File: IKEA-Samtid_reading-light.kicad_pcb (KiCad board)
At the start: 2 copper layers, 21 x 100 mm, 30 parts, among them IC1 ATTINY25-S, P1 CONN_2, U1 MCP1804-SOT23-5, U2 PT4115-SOT89-5

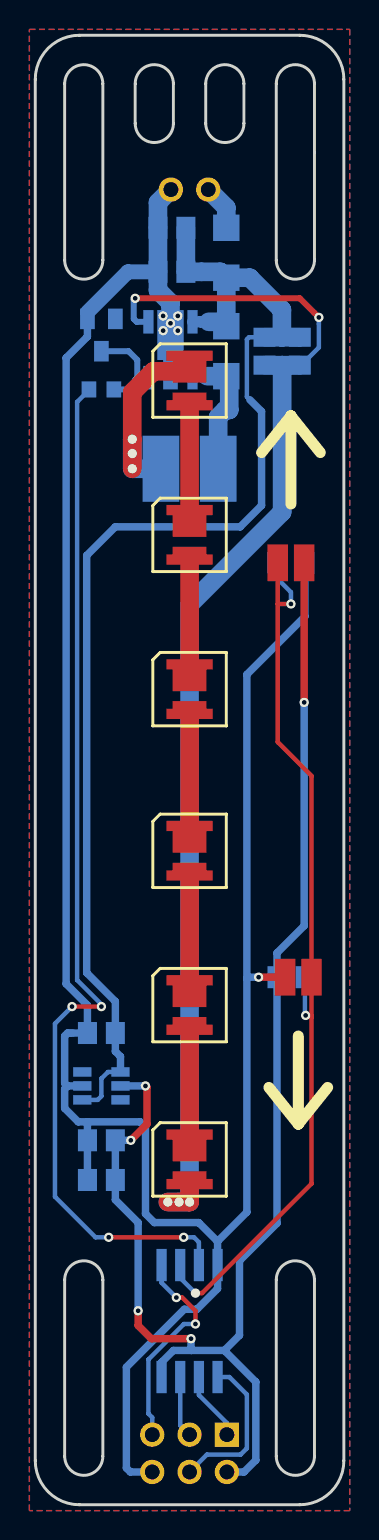
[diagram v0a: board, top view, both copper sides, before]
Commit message: Added a buffer-cap for the ADC input + minor layout tweaks.
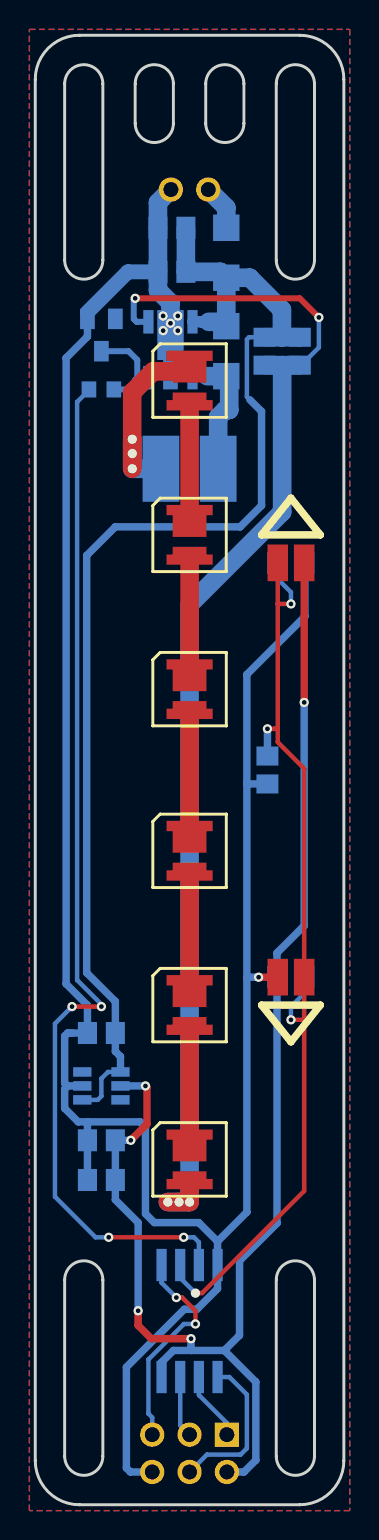
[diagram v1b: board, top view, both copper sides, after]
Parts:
- added C6: 100nF, my_parts:MADW__C0805, B.Cu at (76.3, 88.5)
- moved FSEN2 0.50 mm to (77.9, 102.6)
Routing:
- net /FSEN: track 63.7 -> 67.0 mm, vias 3 -> 4
- net GND: track 99.8 -> 100.8 mm

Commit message: Tweaks.
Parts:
- turned FSEN1 to 180 degrees
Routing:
- net /FSEN: track 67.0 -> 99.2 mm, vias 4 -> 2
- net GND: track 100.8 -> 102.2 mm
- net +5V: track 97.1 -> 98.1 mm
- net +24V: track 87.3 -> 86.3 mm

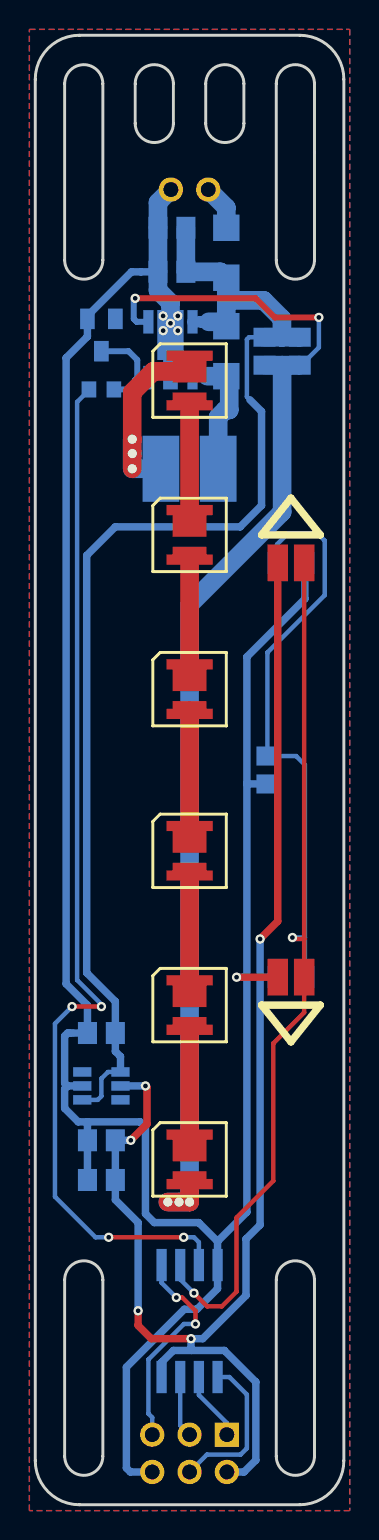
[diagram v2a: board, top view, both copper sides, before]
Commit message: Moved sensor pads away from LEDs + improved power input footprint.
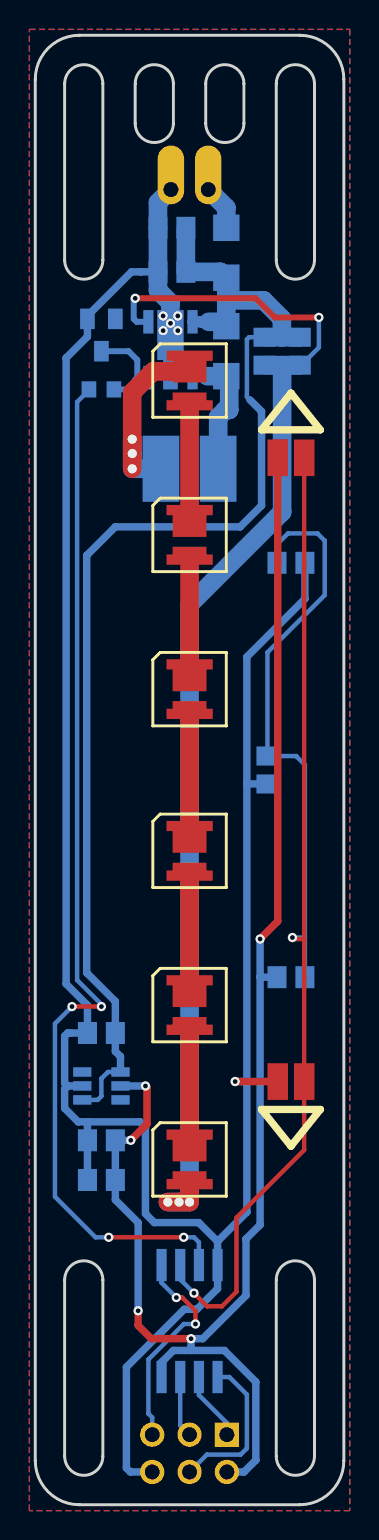
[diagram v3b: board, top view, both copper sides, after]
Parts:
- moved FSEN1 7.15 mm to (77.9, 67.2)
- moved FSEN2 7.10 mm to (77.9, 109.7)
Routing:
- net /FSEN: track 99.2 -> 106.4 mm
- net +5V: track 98.1 -> 105.3 mm
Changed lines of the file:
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@@
     (thickness 1.6002)
     (drawings 70)
-    (tracks 278)
+    (tracks 279)
     (zones 0)
     (modules 31)
@@
   )
   (setup
-    (last_trace_width 1.27)
+    (last_trace_width 0.2032)
     (user_trace_width 0.2032)
     (user_trace_width 0.3048)
@@
     (mod_text_size 1 1)
     (mod_text_width 0.2)
-    (pad_size 0.85 0.85)
-    (pad_drill 0.35)
+    (pad_size 4 1.8)
+    (pad_drill 1.016)
     (pad_to_mask_clearance 0)
     (aux_axis_origin 0 0)
@@
     (add_net "Net-(D6-Pad2)")
     (add_net "Net-(DS1-Pad1)")
+  )
+  (module my_parts:MADW__edge-connector_SIL2_male (layer Back)
+    (at 71 49 270)
+    (clearance 0.5)
+    (fp_text reference P1 (at 0 3.81 270) (layer B.SilkS) hide
+      (effects (font (size 1 1) (thickness 0.2)) (justify mirror))
+    )
+    (fp_text value CONN_2 (at 0 -3.81 270) (layer B.SilkS) hide
+      (effects (font (size 1 1) (thickness 0.2)) (justify mirror))
+    )
+    (fp_line (start -1.4 -2.54) (end -1.4 2.54) (layer B.SilkS) (width 0.2))
+    (fp_line (start -3.9 2.54) (end -3.9 -2.54) (layer B.SilkS) (width 0.2))
+    (fp_line (start -1.39954 2.54) (end -3.8989 2.54) (layer B.SilkS) (width 0.2))
+    (fp_line (start -3.8989 -1.27) (end -9.90092 -1.27) (layer B.SilkS) (width 0.2))
+    (fp_line (start -3.8989 1.27) (end -9.90092 1.27) (layer B.SilkS) (width 0.2))
+    (fp_line (start -1.39954 0) (end -3.8989 0) (layer B.SilkS) (width 0.2))
+    (fp_line (start -1.39954 -2.54) (end -3.8989 -2.54) (layer B.SilkS) (width 0.2))
+    (pad 2 thru_hole oval (at 0 -1.27 270) (size 4 1.8) (drill 1.016 (offset -1 0)) (layers *.Cu *.Mask B.SilkS)
+      (net 20 "Net-(DS1-Pad1)"))
+    (pad 1 thru_hole oval (at 0 1.27 270) (size 4 1.8) (drill 1.016 (offset -1 0)) (layers *.Cu *.Mask B.SilkS)
+      (net 19 GNDPWR) (zone_connect 1) (thermal_gap 0.5))
+    (model ../../../../../Arduino/KiCAD/kicad_sources/library-repos/kicad-library/modules/packages3d/Pin_Headers/Pin_Header_Angled_1x02.wrl
+      (at (xyz 0 0 0))
+      (scale (xyz 1 1 1))
+      (rotate (xyz 0 0 -90))
+    )
   )
   (module my_parts:MADW__SOT89-5 (layer Back)
@@
   )
   (module my_parts:MADW__SMD_2-pin_square_3.2x2.5mm (layer Front)
-    (at 77.9 102.6)
+    (at 77.9 109.7)
     (tags "CONN DEV")
     (clearance 0.4)
@@
   )
   (module my_parts:MADW__SMD_2-pin_square_3.2x2.5mm (layer Front)
-    (at 77.9 74.4 180)
+    (at 77.9 67.25 180)
     (tags "CONN DEV")
     (clearance 0.4)
@@
     (pad 1 smd rect (at 0.9 0 180) (size 1.4 2.5) (layers Front F.Paste F.Mask)
       (net 9 +5V))
-  )
-  (module my_parts:MADW__edge-connector_SIL2_male (layer Back)
-    (at 71 49 270)
-    (fp_text reference P1 (at 0 3.81 270) (layer B.SilkS) hide
-      (effects (font (size 1 1) (thickness 0.2)) (justify mirror))
-    )
-    (fp_text value CONN_2 (at 0 -3.81 270) (layer B.SilkS) hide
-      (effects (font (size 1 1) (thickness 0.2)) (justify mirror))
-    )
-    (fp_line (start -1.4 -2.54) (end -1.4 2.54) (layer B.SilkS) (width 0.2))
-    (fp_line (start -3.9 2.54) (end -3.9 -2.54) (layer B.SilkS) (width 0.2))
-    (fp_line (start -1.39954 2.54) (end -3.8989 2.54) (layer B.SilkS) (width 0.2))
-    (fp_line (start -3.8989 -1.27) (end -9.90092 -1.27) (layer B.SilkS) (width 0.2))
-    (fp_line (start -3.8989 1.27) (end -9.90092 1.27) (layer B.SilkS) (width 0.2))
-    (fp_line (start -1.39954 0) (end -3.8989 0) (layer B.SilkS) (width 0.2))
-    (fp_line (start -1.39954 -2.54) (end -3.8989 -2.54) (layer B.SilkS) (width 0.2))
-    (pad 2 thru_hole circle (at 0 -1.27 270) (size 1.651 1.651) (drill 1.016) (layers *.Cu *.Mask B.SilkS)
-      (net 20 "Net-(DS1-Pad1)"))
-    (pad 1 thru_hole circle (at 0 1.27 270) (size 1.651 1.651) (drill 1.016) (layers *.Cu *.Mask B.SilkS)
-      (net 19 GNDPWR))
-    (model ../../../../../Arduino/KiCAD/kicad_sources/library-repos/kicad-library/modules/packages3d/Pin_Headers/Pin_Header_Angled_1x02.wrl
-      (at (xyz 0 0 0))
-      (scale (xyz 1 1 1))
-      (rotate (xyz 0 0 -90))
-    )
   )
   (module my_parts:MADW__SMD-net-noin-0.5mm (layer Back)
@@
       (net 1 GND))
   )
-  (gr_line (start 75.9 72.5) (end 79.9 72.5) (layer F.SilkS) (width 0.5))
+  (gr_line (start 75.9 65.35) (end 79.9 65.35) (layer F.SilkS) (width 0.5))
   (gr_arc (start 68.6 41.8) (end 67.3 41.8) (angle 180) (layer Edge.Cuts) (width 0.2))
   (gr_line (start 67.3 44.5) (end 67.3 41.8) (layer Edge.Cuts) (width 0.2))
@@
   (gr_arc (start 68.6 44.5) (end 69.9 44.5) (angle 180) (layer Eco1.User) (width 0.2))
   (gr_arc (start 73.4 44.5) (end 74.7 44.5) (angle 180) (layer Eco1.User) (width 0.2))
-  (gr_line (start 77.9 70) (end 75.9 72.5) (angle 90) (layer F.SilkS) (width 0.5))
-  (gr_line (start 77.9 70) (end 79.9 72.5) (angle 90) (layer F.SilkS) (width 0.5))
-  (gr_line (start 77.9 107) (end 79.9 104.5) (layer F.SilkS) (width 0.5))
-  (gr_line (start 77.9 107) (end 75.9 104.5) (layer F.SilkS) (width 0.5))
-  (gr_line (start 79.9 104.5) (end 75.9 104.5) (layer F.SilkS) (width 0.5))
+  (gr_line (start 77.9 62.85) (end 75.9 65.35) (angle 90) (layer F.SilkS) (width 0.5))
+  (gr_line (start 77.9 62.85) (end 79.9 65.35) (angle 90) (layer F.SilkS) (width 0.5))
+  (gr_line (start 77.9 114.1) (end 79.9 111.6) (layer F.SilkS) (width 0.5))
+  (gr_line (start 77.9 114.1) (end 75.9 111.6) (layer F.SilkS) (width 0.5))
+  (gr_line (start 79.9 111.6) (end 75.9 111.6) (layer F.SilkS) (width 0.5))
   (gr_line (start 79.5 46.458549) (end 79.5 41.8) (layer Edge.Cuts) (width 0.2))
   (dimension 100 (width 0.2) (layer Eco1.User)
@@
   (gr_line (start 63.5 138.5) (end 78.5 138.5) (layer Edge.Cuts) (width 0.2))
   (gr_line (start 60.5 41.5) (end 60.5 135.5) (layer Edge.Cuts) (width 0.2))
-  (segment (start 74.649012 102.6) (end 74.9 102.6) (width 0.508) (layer Back) (net 1))
-  (segment (start 74.2 102.6) (end 74.649012 102.6) (width 0.508) (layer Back) (net 1))
-  (segment (start 77 102.6) (end 74.2 102.6) (width 0.508) (layer Front) (net 1))
-  (via (at 74.2 102.6) (size 0.635) (layers Front Back) (net 1))
+  (segment (start 74.549012 109.7) (end 74.9 109.7) (width 0.508) (layer Back) (net 1))
+  (segment (start 74.1 109.7) (end 74.549012 109.7) (width 0.508) (layer Back) (net 1))
+  (segment (start 77 109.7) (end 74.1 109.7) (width 0.508) (layer Front) (net 1))
+  (via (at 74.1 109.7) (size 0.635) (layers Front Back) (net 1))
   (segment (start 74.9 89.447502) (end 74.9 80.8) (width 0.508) (layer Back) (net 1))
   (segment (start 78.84996 76.85004) (end 78.84996 74.4) (width 0.508) (layer Back) (net 1) (status 20))
@@
   (segment (start 70.365 129.81) (end 70.365 133.095) (width 0.3048) (layer Back) (net 8) (status 10))
   (segment (start 70.365 133.095) (end 71 133.73) (width 0.3048) (layer Back) (net 8) (status 20))
+  (segment (start 77 74.4) (end 77 67.25) (width 0.508) (layer Front) (net 9))
   (segment (start 71.9 127.2) (end 74.840456 124.259544) (width 0.508) (layer Back) (net 9))
   (segment (start 75.8 119.455906) (end 75.8 102.581836) (width 0.508) (layer Back) (net 9))
@@
   (segment (start 65 60) (end 66.84852 60) (width 0.4064) (layer Back) (net 17) (status 10))
   (segment (start 67.44194 60.59342) (end 67.44194 61.79992) (width 0.4064) (layer Back) (net 17))
+  (segment (start 78.8 102.6) (end 78.8 109.7) (width 0.3048) (layer Front) (net 18))
   (segment (start 71.3 124.1) (end 72.2 125) (width 0.3048) (layer Front) (net 18))
   (segment (start 72.2 125) (end 73.2 125) (width 0.3048) (layer Front) (net 18))
   (segment (start 73.2 125) (end 74.2 124) (width 0.3048) (layer Front) (net 18))
   (segment (start 74.2 124) (end 74.2 118.961754) (width 0.3048) (layer Front) (net 18))
-  (segment (start 74.2 118.961754) (end 76.7 116.461754) (width 0.3048) (layer Front) (net 18))
-  (segment (start 76.7 116.461754) (end 76.7 107.1) (width 0.3048) (layer Front) (net 18))
-  (segment (start 76.7 107.1) (end 78.8 105) (width 0.3048) (layer Front) (net 18))
-  (segment (start 78.8 105) (end 78.8 102.6) (width 0.3048) (layer Front) (net 18))
+  (segment (start 74.2 118.961754) (end 78.8 114.361754) (width 0.3048) (layer Front) (net 18))
+  (segment (start 78.8 114.361754) (end 78.8 109.7) (width 0.3048) (layer Front) (net 18))
+  (segment (start 78.8 74.4) (end 78.8 67.25) (width 0.3048) (layer Front) (net 18))
   (segment (start 76.3 87.55004) (end 78.25004 87.55004) (width 0.3048) (layer Back) (net 18) (status 10))
   (segment (start 78.84996 88.14996) (end 78.84996 99.9) (width 0.3048) (layer Back) (net 18))
